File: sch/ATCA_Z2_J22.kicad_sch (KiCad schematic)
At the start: 1 part, among them J11 TE_64690XX-1_J22

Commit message: added magjacks
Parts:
- J11: footprint KIT_Connector:TE_6469001-1 -> project:TE_6469001-1
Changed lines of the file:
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@@
       (effects (font (size 1.27 1.27)))
     )
-    (property "Footprint" "KIT_Connector:TE_6469001-1" (at 191.77 57.15 0)
+    (property "Footprint" "project:TE_6469001-1" (at 191.77 57.15 0)
       (effects (font (size 1.27 1.27)) hide)
     )
@@
       (project "atca_simple_hub"
         (path "/b1bf14e0-f6d2-45a7-b67f-6500a354b7ad/d20dcbe2-daa0-42a8-9881-808161128fb1"
-          (reference "J6") (unit 2)
+          (reference "J22") (unit 2)
         )
       )
@@
       (effects (font (size 1.27 1.27)))
     )
-    (property "Footprint" "KIT_Connector:TE_6469001-1" (at 66.04 135.89 0)
+    (property "Footprint" "project:TE_6469001-1" (at 66.04 135.89 0)
       (effects (font (size 1.27 1.27)) hide)
     )
@@
       (project "atca_simple_hub"
         (path "/b1bf14e0-f6d2-45a7-b67f-6500a354b7ad/d20dcbe2-daa0-42a8-9881-808161128fb1"
-          (reference "J6") (unit 3)
+          (reference "J22") (unit 3)
         )
       )
@@
       (effects (font (size 1.27 1.27)))
     )
-    (property "Footprint" "KIT_Connector:TE_6469001-1" (at 140.97 135.89 0)
+    (property "Footprint" "project:TE_6469001-1" (at 140.97 135.89 0)
       (effects (font (size 1.27 1.27)) hide)
     )
@@
       (project "atca_simple_hub"
         (path "/b1bf14e0-f6d2-45a7-b67f-6500a354b7ad/d20dcbe2-daa0-42a8-9881-808161128fb1"
-          (reference "J6") (unit 4)
+          (reference "J22") (unit 4)
         )
       )
@@
       (effects (font (size 1.27 1.27)))
     )
-    (property "Footprint" "KIT_Connector:TE_6469001-1" (at 227.33 135.89 0)
+    (property "Footprint" "project:TE_6469001-1" (at 227.33 135.89 0)
       (effects (font (size 1.27 1.27)) hide)
     )
@@
       (project "atca_simple_hub"
         (path "/b1bf14e0-f6d2-45a7-b67f-6500a354b7ad/d20dcbe2-daa0-42a8-9881-808161128fb1"
-          (reference "J6") (unit 5)
+          (reference "J22") (unit 5)
         )
       )
@@
       (effects (font (size 1.27 1.27)))
     )
-    (property "Footprint" "KIT_Connector:TE_6469001-1" (at 114.3 57.15 0)
+    (property "Footprint" "project:TE_6469001-1" (at 114.3 57.15 0)
       (effects (font (size 1.27 1.27)) hide)
     )
@@
       (project "atca_simple_hub"
         (path "/b1bf14e0-f6d2-45a7-b67f-6500a354b7ad/d20dcbe2-daa0-42a8-9881-808161128fb1"
-          (reference "J6") (unit 1)
+          (reference "J22") (unit 1)
         )
       )

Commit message: Project recovered
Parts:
- renumbered J11 to J22
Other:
- title: ATCA Template -> ATCA Simple Loopback HUB
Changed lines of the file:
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@@
   (paper "A4")
   (title_block
-    (title "ATCA Template")
-    (date "2023-07-20")
+    (title "ATCA Simple Loopback HUB")
+    (date "2023-09-12")
     (rev "1.0")
     (company "Karlsruhe Institute of Technology (KIT)")
     (comment 1 "Institute for Data Processing and Electronics (IPE)")
     (comment 2 "Luis Ardila")
-    (comment 4 "Licensed under CERN-OHL-S-2.0")
+    (comment 3 "IPE-380-06")
+    (comment 4 "Licensed under CERN-OHL-P-2.0")
   )
   (junction (at 212.09 67.31) (diameter 0) (color 0 0 0 0)
@@
   (symbol (lib_id "power:GND") (at 212.09 72.39 0) (unit 1)
     (in_bom yes) (on_board yes) (dnp no)
-    (property "Reference" "#PWR0731" (at 212.09 78.74 0)
+    (property "Reference" "#PWR046" (at 212.09 78.74 0)
       (effects (font (size 1.27 1.27)) hide)
     )
@@
     (pin "1")
     (instances
-      (project "atca_simple_hub"
+      (project "atca-simple-loopback-hub"
         (path "/b1bf14e0-f6d2-45a7-b67f-6500a354b7ad/d20dcbe2-daa0-42a8-9881-808161128fb1"
           (reference "#PWR046") (unit 1)
@@
   (symbol (lib_id "power:GND") (at 86.36 151.13 0) (unit 1)
     (in_bom yes) (on_board yes) (dnp no)
-    (property "Reference" "#PWR0483" (at 86.36 157.48 0)
+    (property "Reference" "#PWR047" (at 86.36 157.48 0)
       (effects (font (size 1.27 1.27)) hide)
     )
@@
     (pin "1")
     (instances
-      (project "atca_simple_hub"
+      (project "atca-simple-loopback-hub"
         (path "/b1bf14e0-f6d2-45a7-b67f-6500a354b7ad/d20dcbe2-daa0-42a8-9881-808161128fb1"
           (reference "#PWR047") (unit 1)
@@
   (symbol (lib_id "project:TE_64690XX-1_J22") (at 191.77 57.15 0) (unit 2)
     (in_bom yes) (on_board yes) (dnp no) (fields_autoplaced)
-    (property "Reference" "J11" (at 191.77 26.67 0)
+    (property "Reference" "J22" (at 191.77 26.67 0)
       (effects (font (size 1.27 1.27)))
     )
@@
     (pin "9HG")
     (instances
-      (project "atca_simple_hub"
+      (project "atca-simple-loopback-hub"
         (path "/b1bf14e0-f6d2-45a7-b67f-6500a354b7ad/d20dcbe2-daa0-42a8-9881-808161128fb1"
           (reference "J22") (unit 2)
@@
   (symbol (lib_id "project:TE_64690XX-1_J22") (at 66.04 135.89 0) (unit 3)
     (in_bom yes) (on_board yes) (dnp no) (fields_autoplaced)
-    (property "Reference" "J11" (at 66.04 105.41 0)
+    (property "Reference" "J22" (at 66.04 105.41 0)
       (effects (font (size 1.27 1.27)))
     )
@@
     (pin "9HG")
     (instances
-      (project "atca_simple_hub"
+      (project "atca-simple-loopback-hub"
         (path "/b1bf14e0-f6d2-45a7-b67f-6500a354b7ad/d20dcbe2-daa0-42a8-9881-808161128fb1"
           (reference "J22") (unit 3)
@@
   (symbol (lib_id "project:TE_64690XX-1_J22") (at 140.97 135.89 0) (unit 4)
     (in_bom yes) (on_board yes) (dnp no) (fields_autoplaced)
-    (property "Reference" "J11" (at 140.97 105.41 0)
+    (property "Reference" "J22" (at 140.97 105.41 0)
       (effects (font (size 1.27 1.27)))
     )
@@
     (pin "9HG")
     (instances
-      (project "atca_simple_hub"
+      (project "atca-simple-loopback-hub"
         (path "/b1bf14e0-f6d2-45a7-b67f-6500a354b7ad/d20dcbe2-daa0-42a8-9881-808161128fb1"
           (reference "J22") (unit 4)
@@
   (symbol (lib_id "project:TE_64690XX-1_J22") (at 227.33 135.89 0) (unit 5)
     (in_bom yes) (on_board yes) (dnp no) (fields_autoplaced)
-    (property "Reference" "J11" (at 227.33 105.41 0)
+    (property "Reference" "J22" (at 227.33 105.41 0)
       (effects (font (size 1.27 1.27)))
     )
@@
     (pin "9HG")
     (instances
-      (project "atca_simple_hub"
+      (project "atca-simple-loopback-hub"
         (path "/b1bf14e0-f6d2-45a7-b67f-6500a354b7ad/d20dcbe2-daa0-42a8-9881-808161128fb1"
           (reference "J22") (unit 5)
@@
   (symbol (lib_id "power:GND") (at 161.29 151.13 0) (unit 1)
     (in_bom yes) (on_board yes) (dnp no)
-    (property "Reference" "#PWR0730" (at 161.29 157.48 0)
+    (property "Reference" "#PWR048" (at 161.29 157.48 0)
       (effects (font (size 1.27 1.27)) hide)
     )
@@
     (pin "1")
     (instances
-      (project "atca_simple_hub"
+      (project "atca-simple-loopback-hub"
         (path "/b1bf14e0-f6d2-45a7-b67f-6500a354b7ad/d20dcbe2-daa0-42a8-9881-808161128fb1"
           (reference "#PWR048") (unit 1)
@@
   (symbol (lib_id "project:TE_64690XX-1_J22") (at 114.3 57.15 0) (unit 1)
     (in_bom yes) (on_board yes) (dnp no) (fields_autoplaced)
-    (property "Reference" "J11" (at 114.3 26.67 0)
+    (property "Reference" "J22" (at 114.3 26.67 0)
       (effects (font (size 1.27 1.27)))
     )
@@
     (pin "9HG")
     (instances
-      (project "atca_simple_hub"
+      (project "atca-simple-loopback-hub"
         (path "/b1bf14e0-f6d2-45a7-b67f-6500a354b7ad/d20dcbe2-daa0-42a8-9881-808161128fb1"
           (reference "J22") (unit 1)
@@
   (symbol (lib_id "power:GND") (at 134.62 72.39 0) (unit 1)
     (in_bom yes) (on_board yes) (dnp no)
-    (property "Reference" "#PWR0482" (at 134.62 78.74 0)
+    (property "Reference" "#PWR045" (at 134.62 78.74 0)
       (effects (font (size 1.27 1.27)) hide)
     )
@@
     (pin "1")
     (instances
-      (project "atca_simple_hub"
+      (project "atca-simple-loopback-hub"
         (path "/b1bf14e0-f6d2-45a7-b67f-6500a354b7ad/d20dcbe2-daa0-42a8-9881-808161128fb1"
           (reference "#PWR045") (unit 1)
@@
   (symbol (lib_id "power:GND") (at 247.65 151.13 0) (unit 1)
     (in_bom yes) (on_board yes) (dnp no)
-    (property "Reference" "#PWR0734" (at 247.65 157.48 0)
+    (property "Reference" "#PWR049" (at 247.65 157.48 0)
       (effects (font (size 1.27 1.27)) hide)
     )
@@
     (pin "1")
     (instances
-      (project "atca_simple_hub"
+      (project "atca-simple-loopback-hub"
         (path "/b1bf14e0-f6d2-45a7-b67f-6500a354b7ad/d20dcbe2-daa0-42a8-9881-808161128fb1"
           (reference "#PWR049") (unit 1)

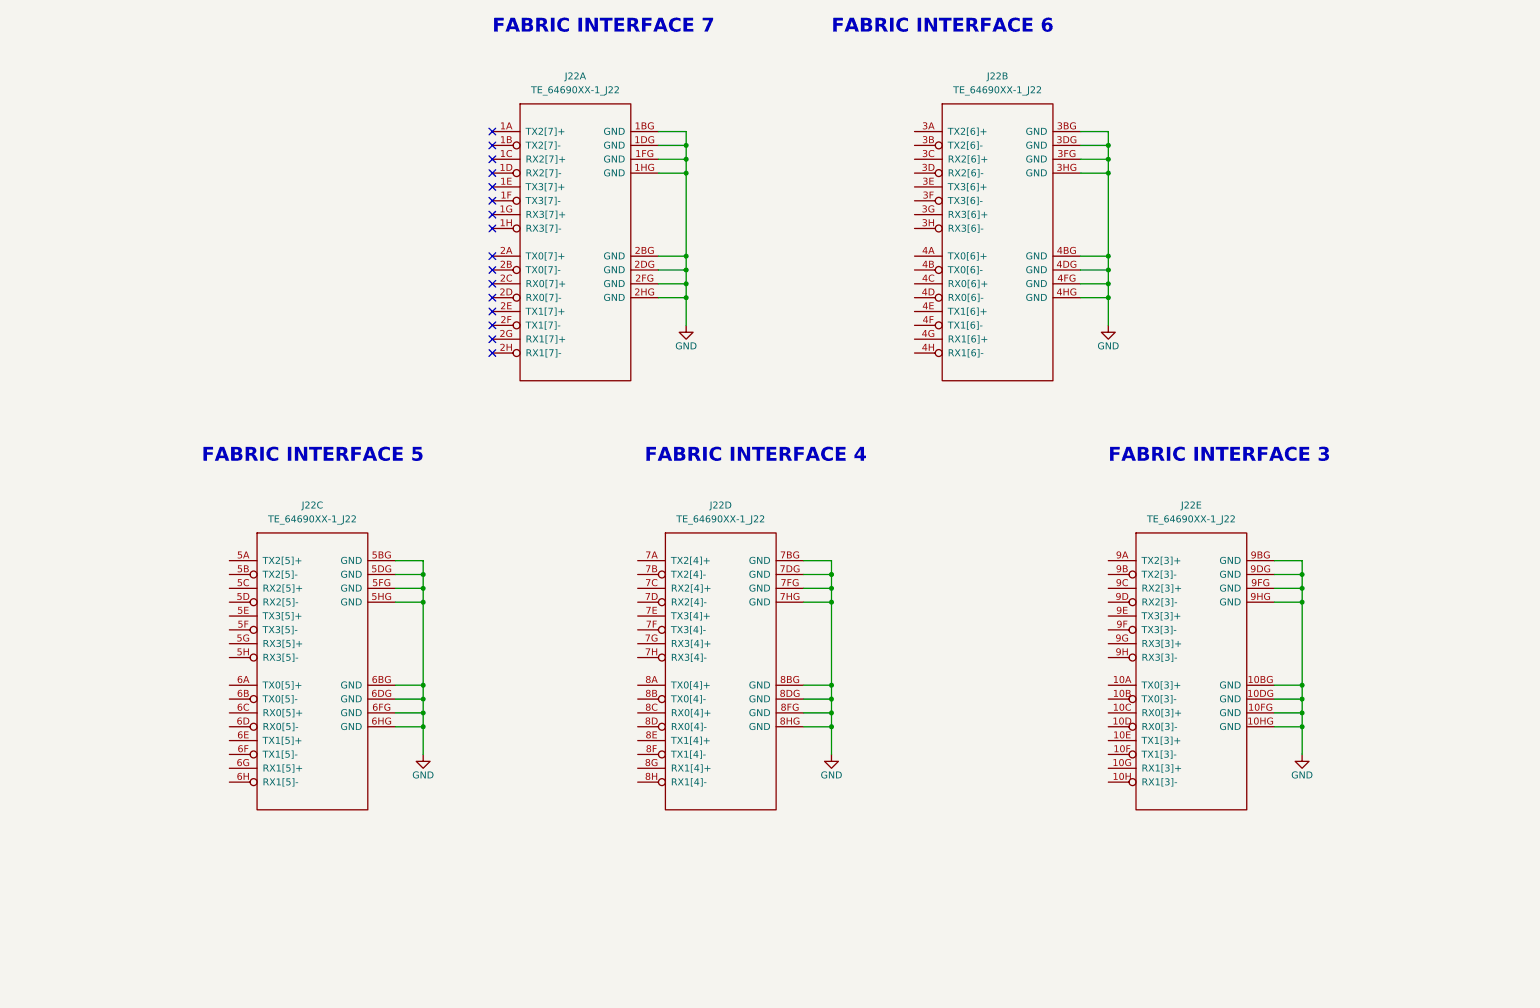
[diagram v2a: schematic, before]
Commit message: organization of sub sheets
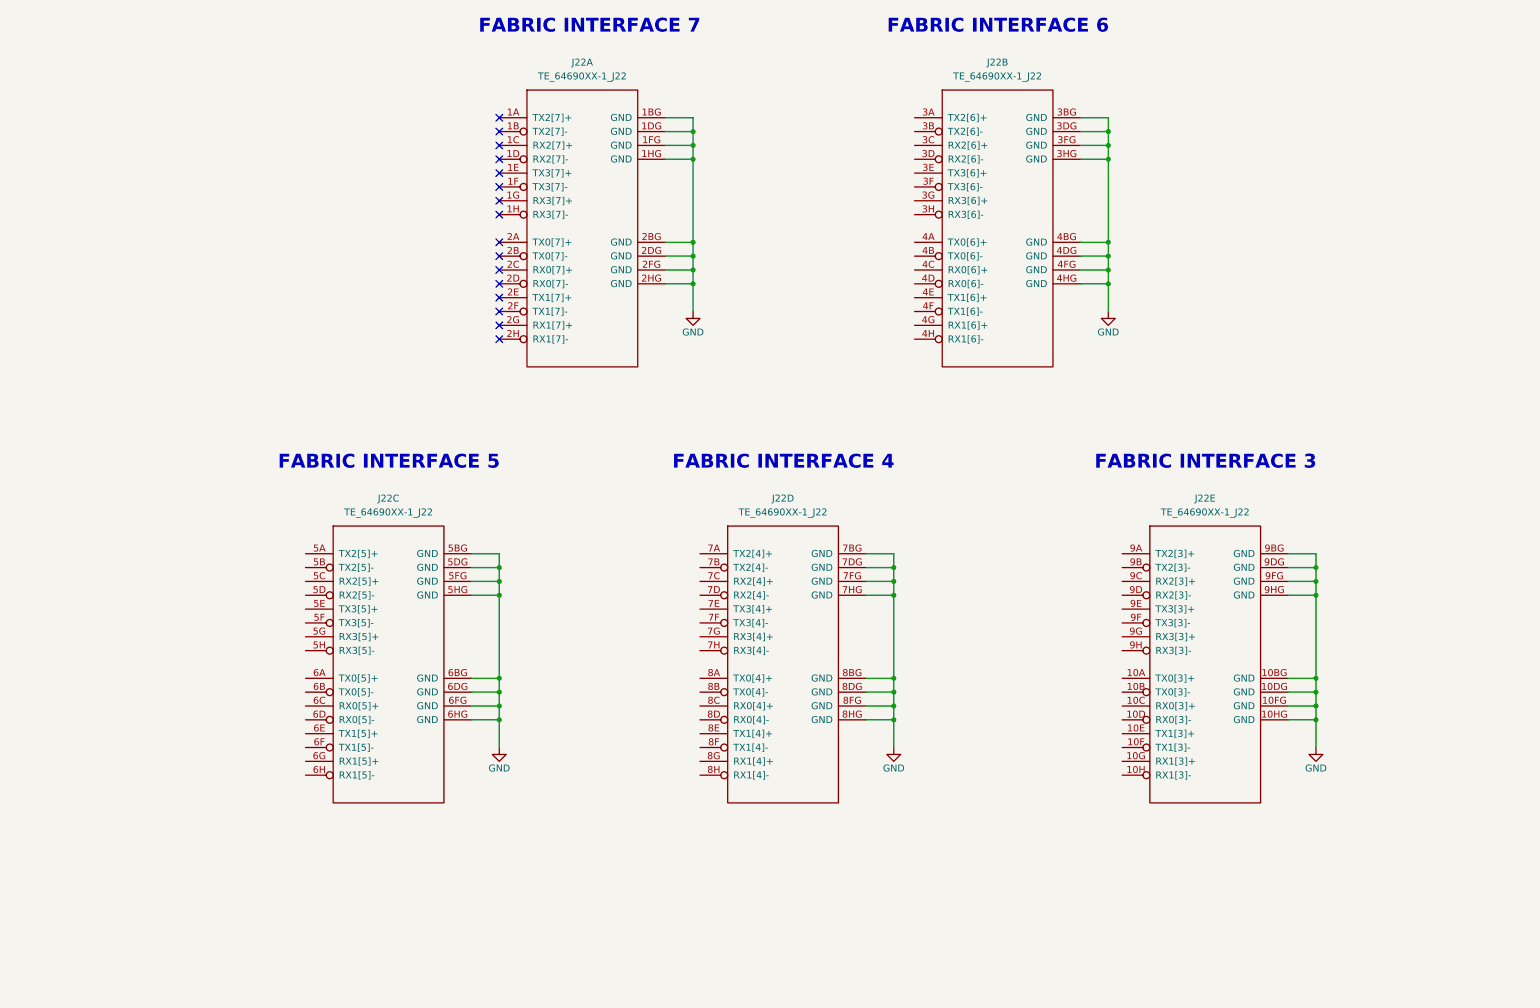
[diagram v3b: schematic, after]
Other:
- moved on the sheet: J22A, J22B, J22C, J22D, J22E
